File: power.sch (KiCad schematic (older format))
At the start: 38 parts, among them Q2 NC, Q3 TPS27082L, Q4 Q_NMOS_DGS, U3 RT8070, U4 TLV70218DBVR

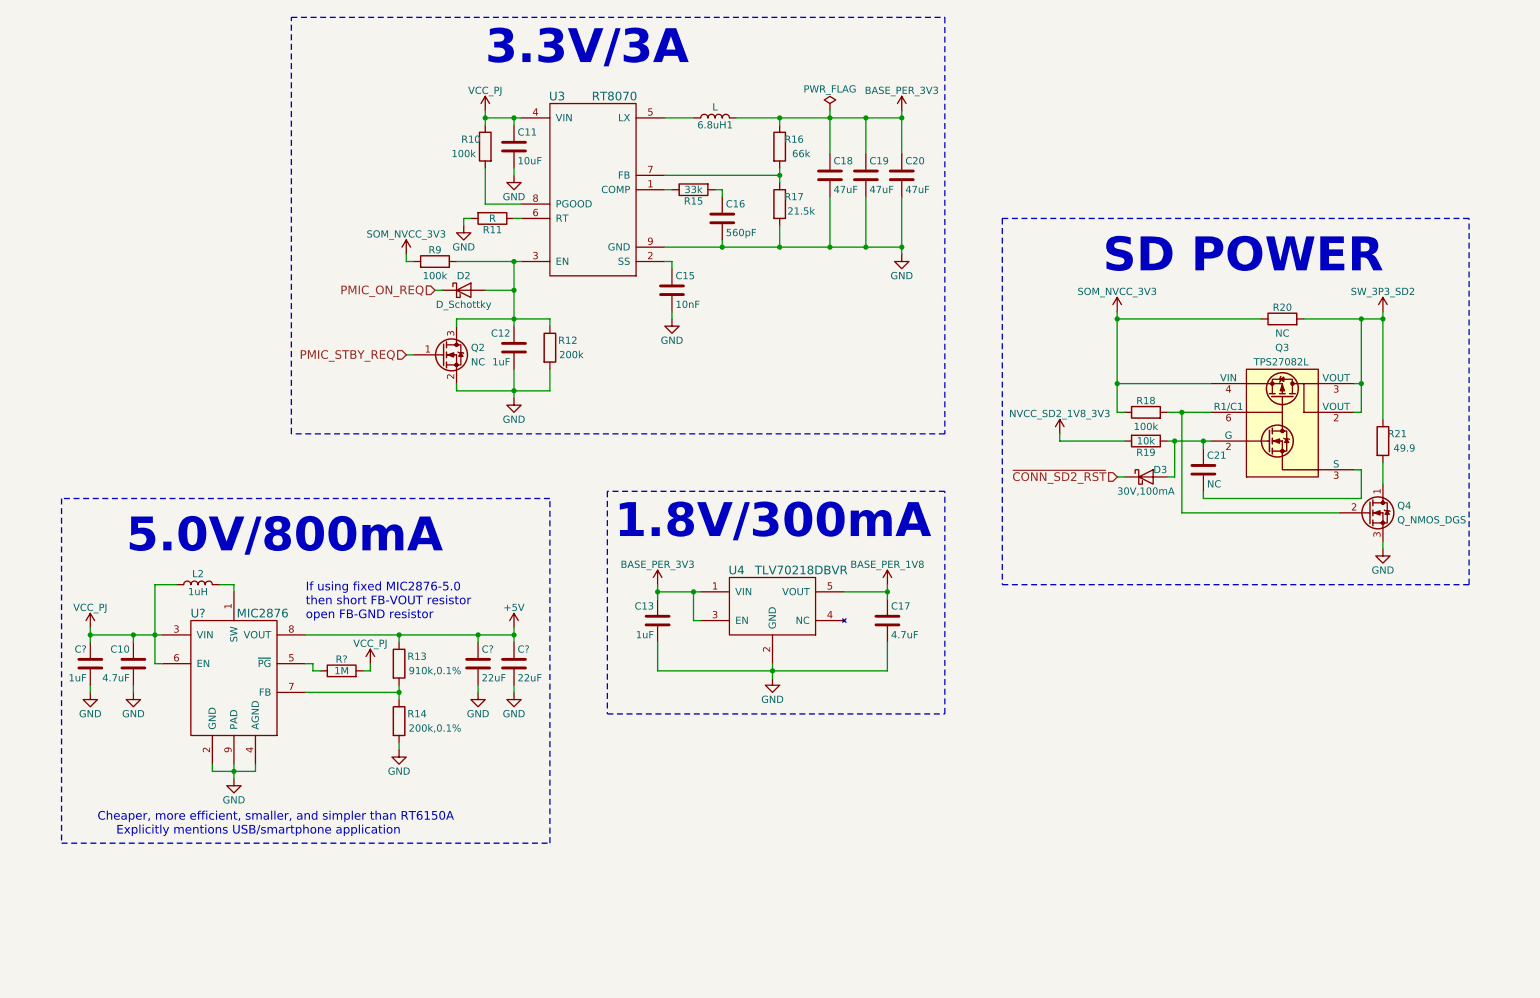
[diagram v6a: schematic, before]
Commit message: Use a buck for the 1.8V rail for efficiency, include power line ferrite bead, change main buck-boost output caps to 0805 ones, move the main regulator's input caps to the VIN node, include USB power switch circuit's components
The 1.8V buck has a drop-in: "ST1S12G18R"
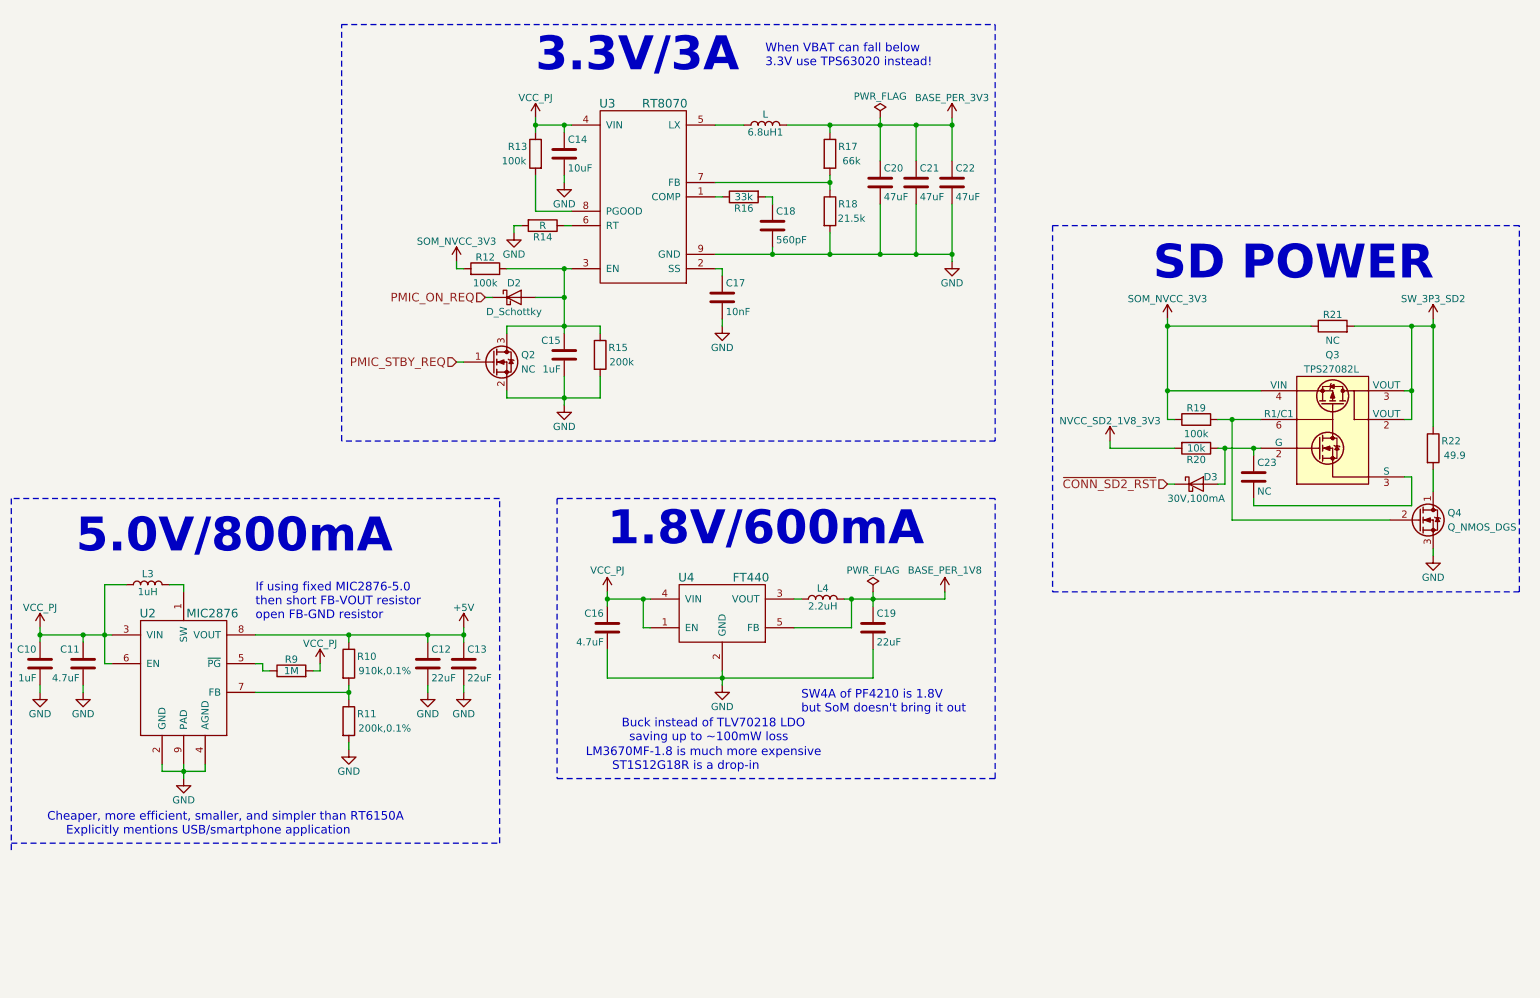
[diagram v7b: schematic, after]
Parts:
- removed C13: 1uF, symbol C
- removed C17: 4.7uF, symbol C
- removed U4: TLV70218DBVR, symbol TLV70218DBVR
- added C16: 4.7uF, symbol C
- added C19: 22uF, Capacitors_SMD:C_0805, symbol C
- added L4: 2.2uH, symbol L
- added U4: FT440, symbol FT440
- C12, C13: renamed from C?; Distrib Link https://www.digikey.com/product-detail/en/taiyo-yuden/LMK21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 -> https://www.mouser.com/ProductDetail/Taiyo-Yuden/LMK212BBJ2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
- gave numbers to parts that had none: 3
- renumbered C10 to C11, C11 to C14, C12 to C15, C15 to C17, C16 to C18, C18 to C20, C19 to C21, C20 to C22, C21 to C23, L2 to L3, R13 to R10, R14 to R11, R9 to R12, R10 to R13, R11 to R14, R12 to R15, R15 to R16, R16 to R17, R17 to R18, R18 to R19, R19 to R20, R20 to R21, R21 to R22
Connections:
- net BASE_PER_1V8: now also C19.1, L4.2, U4.5 (FB)
- net GND: now also C16.2, C19.2, U4.2 (GND)
- net VCC_PJ: now also C16.1, U4.1 (EN), U4.4 (VIN)
- new net: L4.1, U4.3 (VOUT)
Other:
- note added: "1.8V/600mA"
- note added: "Buck instead of TLV70218 LDO\n saving up to ~~100mW loss"
- note added: "LM3670MF-1.8 is much more expensive\n ST1S12G18R is a drop-in"
- note added: "SW4A of PF4210 is 1.8V\nbut SoM doesn't bring it out"
- note added: "When VBAT can fall below\n3.3V use TPS63020 instead!"
- note removed: "1.8V/300mA"
- moved on the sheet: 6.8uH1, C10, C11, C12, C13, C14, C15, C17, C18, C20, C21, C22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

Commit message: Include uSD card schematic, add note about testing 1.8V LDO in place of the buck
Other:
- note added: "When VCC_PJ≅VBAT\nLDO can be tested"
- note added: "~~129.9ms until\n≥VIH (1.6V)"
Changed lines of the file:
@@
 $Descr A4 11693 8268
 encoding utf-8
-Sheet 3 7
+Sheet 3 8
 Title "Power"
 Date "2018-04-05"
@@
 Text Notes 6100 5650 0    60   ~ 0
   SW4A of PF4210 is 1.8V\nbut SoM doesn't bring it out
+Text Notes 6500 5950 0    60   ~ 0
+When VCC_PJ≅VBAT\nLDO can be tested
+Text Notes 4550 2900 0    60   ~ 0
+~~129.9ms until\n≥VIH (1.6V)
 $EndSCHEMATC
